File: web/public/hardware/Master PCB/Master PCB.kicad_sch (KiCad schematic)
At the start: 42 parts, among them J1 SWD Conn, SW1 nRST, U1 STM32U585VITx

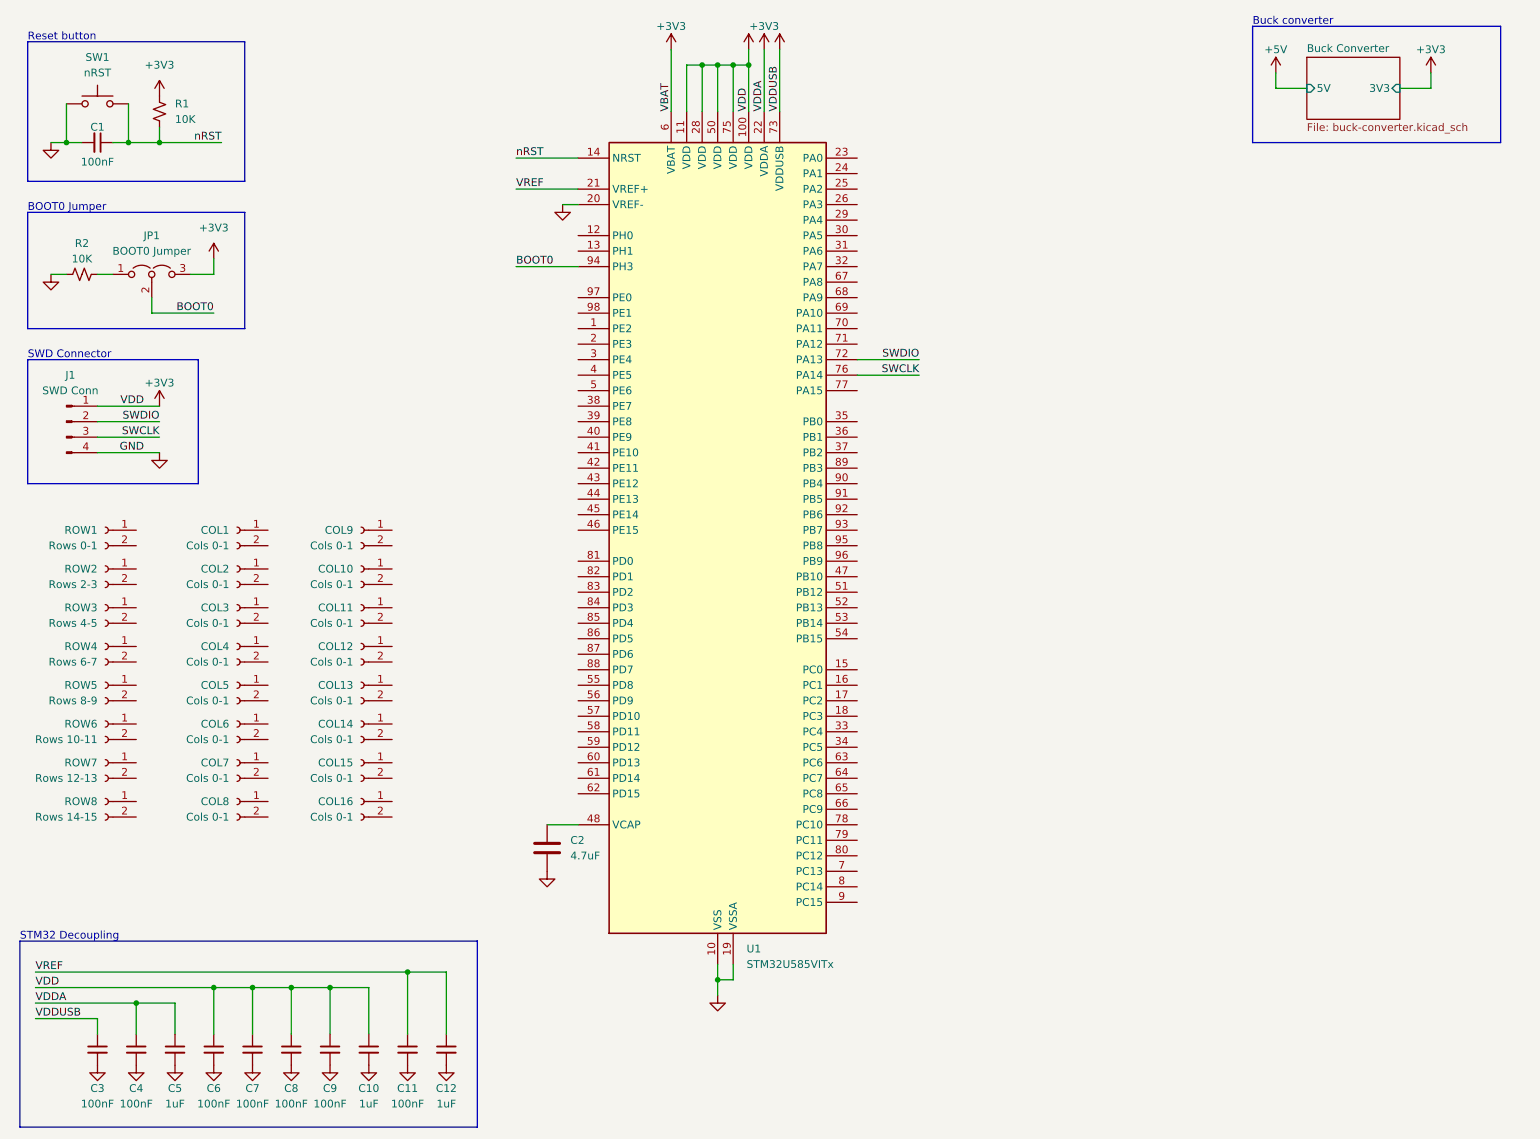
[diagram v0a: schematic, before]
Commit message: Add row/column headers, some hierarchical sheets
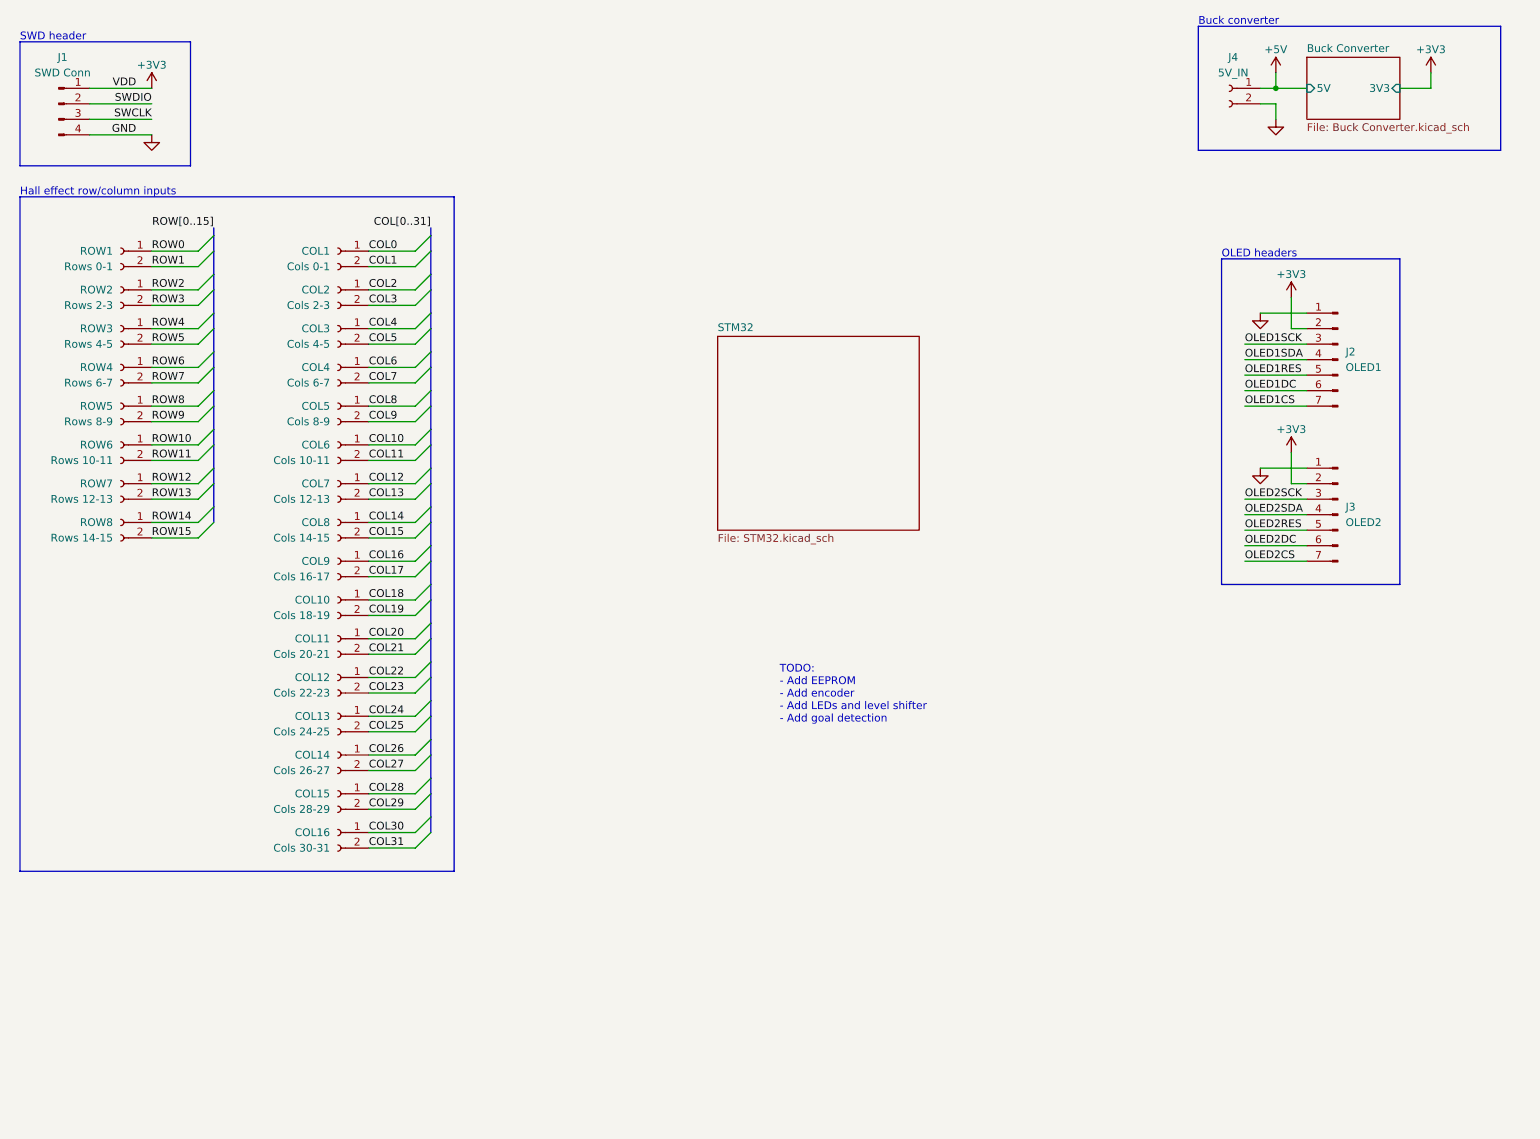
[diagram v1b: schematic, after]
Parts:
- removed C1, C11, C3, C4, C6, C7, C8, C9: 100nF, symbol Device:C_Small
- removed C10, C12, C5: 1uF, symbol Device:C_Small
- removed C2: 4.7uF, symbol Device:C
- removed JP1: BOOT0 Jumper, symbol Jumper:Jumper_3_Open
- removed R1, R2: 10K, symbol Device:R_Small_US
- removed SW1: nRST, symbol Switch:SW_Push
- removed U1: STM32U585VITx, Package_QFP:LQFP-100_14x14mm_P0.5mm, symbol MCU_ST_STM32U5:STM32U585VITx
- added J2: OLED1, symbol Connector:Conn_01x07_Pin
- added J3: OLED2, symbol Connector:Conn_01x07_Pin
- added J4: 5V_IN, symbol Connector:Conn_01x02_Socket
- COL10: value Cols 0-1 -> Cols 18-19
- COL11: value Cols 0-1 -> Cols 20-21
- COL12: value Cols 0-1 -> Cols 22-23
- COL13: value Cols 0-1 -> Cols 24-25
- COL14: value Cols 0-1 -> Cols 26-27
- COL15: value Cols 0-1 -> Cols 28-29
- COL16: value Cols 0-1 -> Cols 30-31
- COL2: value Cols 0-1 -> Cols 2-3
- COL3: value Cols 0-1 -> Cols 4-5
- COL4: value Cols 0-1 -> Cols 6-7
- COL5: value Cols 0-1 -> Cols 8-9
- COL6: value Cols 0-1 -> Cols 10-11
- COL7: value Cols 0-1 -> Cols 12-13
- COL8: value Cols 0-1 -> Cols 14-15
- COL9: value Cols 0-1 -> Cols 16-17
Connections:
- net +3V3: now also J2.2 (Pin_2), J3.2 (Pin_2)
- net +5V: now also J4.1 (Pin_1)
- net GND: now also J2.1 (Pin_1), J3.1 (Pin_1), J4.2 (Pin_2)
- net ROW6: now reaches ROW4.1 (Pin_1)
- net ROW7: now reaches ROW4.2 (Pin_2)
- net ROW2: now reaches ROW2.1 (Pin_1)
- net ROW3: now reaches ROW2.2 (Pin_2)
- net ROW10: now reaches ROW6.1 (Pin_1)
- net ROW11: now reaches ROW6.2 (Pin_2)
- net COL0: now reaches COL1.1 (Pin_1)
- net COL1: now reaches COL1.2 (Pin_2)
- net COL2: now reaches COL2.1 (Pin_1)
- net COL3: now reaches COL2.2 (Pin_2)
- net COL12: now reaches COL7.1 (Pin_1)
- net COL13: now reaches COL7.2 (Pin_2)
- net COL24: now reaches COL13.1 (Pin_1)
- net COL25: now reaches COL13.2 (Pin_2)
- net ROW0: now reaches ROW1.1 (Pin_1)
- net ROW1: now reaches ROW1.2 (Pin_2)
- net COL10: now reaches COL6.1 (Pin_1)
- net COL11: now reaches COL6.2 (Pin_2)
- net COL22: now reaches COL12.1 (Pin_1)
- net COL23: now reaches COL12.2 (Pin_2)
- net COL26: now reaches COL14.1 (Pin_1)
- net COL27: now reaches COL14.2 (Pin_2)
- net COL8: now reaches COL5.1 (Pin_1)
- net COL9: now reaches COL5.2 (Pin_2)
- net COL28: now reaches COL15.1 (Pin_1)
- net COL29: now reaches COL15.2 (Pin_2)
- net ROW12: now reaches ROW7.1 (Pin_1)
- net ROW13: now reaches ROW7.2 (Pin_2)
- net COL18: now reaches COL10.1 (Pin_1)
- net COL19: now reaches COL10.2 (Pin_2)
- net COL4: now reaches COL3.1 (Pin_1)
- net COL5: now reaches COL3.2 (Pin_2)
- net ROW14: now reaches ROW8.1 (Pin_1)
- net ROW15: now reaches ROW8.2 (Pin_2)
- net ROW4: now reaches ROW3.1 (Pin_1)
- net ROW5: now reaches ROW3.2 (Pin_2)
- net COL20: now reaches COL11.1 (Pin_1)
- net COL21: now reaches COL11.2 (Pin_2)
- net COL6: now reaches COL4.1 (Pin_1)
- net COL7: now reaches COL4.2 (Pin_2)
- net COL16: now reaches COL9.1 (Pin_1)
- net COL17: now reaches COL9.2 (Pin_2)
- net ROW8: now reaches ROW5.1 (Pin_1)
- net ROW9: now reaches ROW5.2 (Pin_2)
- net COL14: now reaches COL8.1 (Pin_1)
- net COL15: now reaches COL8.2 (Pin_2)
- net COL30: now reaches COL16.1 (Pin_1)
- net COL31: now reaches COL16.2 (Pin_2)
- new net OLED1CS: J2.7 (Pin_7)
- new net OLED1DC: J2.6 (Pin_6)
- new net OLED1RES: J2.5 (Pin_5)
- new net OLED1SCK: J2.3 (Pin_3)
- new net OLED1SDA: J2.4 (Pin_4)
- new net OLED2CS: J3.7 (Pin_7)
- new net OLED2DC: J3.6 (Pin_6)
- new net OLED2RES: J3.5 (Pin_5)
- new net OLED2SCK: J3.3 (Pin_3)
- new net OLED2SDA: J3.4 (Pin_4)
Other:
- added sheet STM32 (STM32.kicad_sch)
- sheet Buck Converter: file buck-converter.kicad_sch -> Buck Converter.kicad_sch
- note added: "Hall effect row/column inputs"
- note added: "OLED headers"
- note added: "SWD header"
- note added: "TODO: - Add EEPROM - Add encoder - Add LEDs and level shifter - Add goal detection"
- note removed: "BOOT0 Jumper"
- note removed: "Reset button"
- note removed: "STM32 Decoupling"
- note removed: "SWD Connector"
- moved on the sheet: COL1, COL10, COL11, COL12, COL13, COL14, COL15, COL16, COL2, COL3, COL4, COL5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

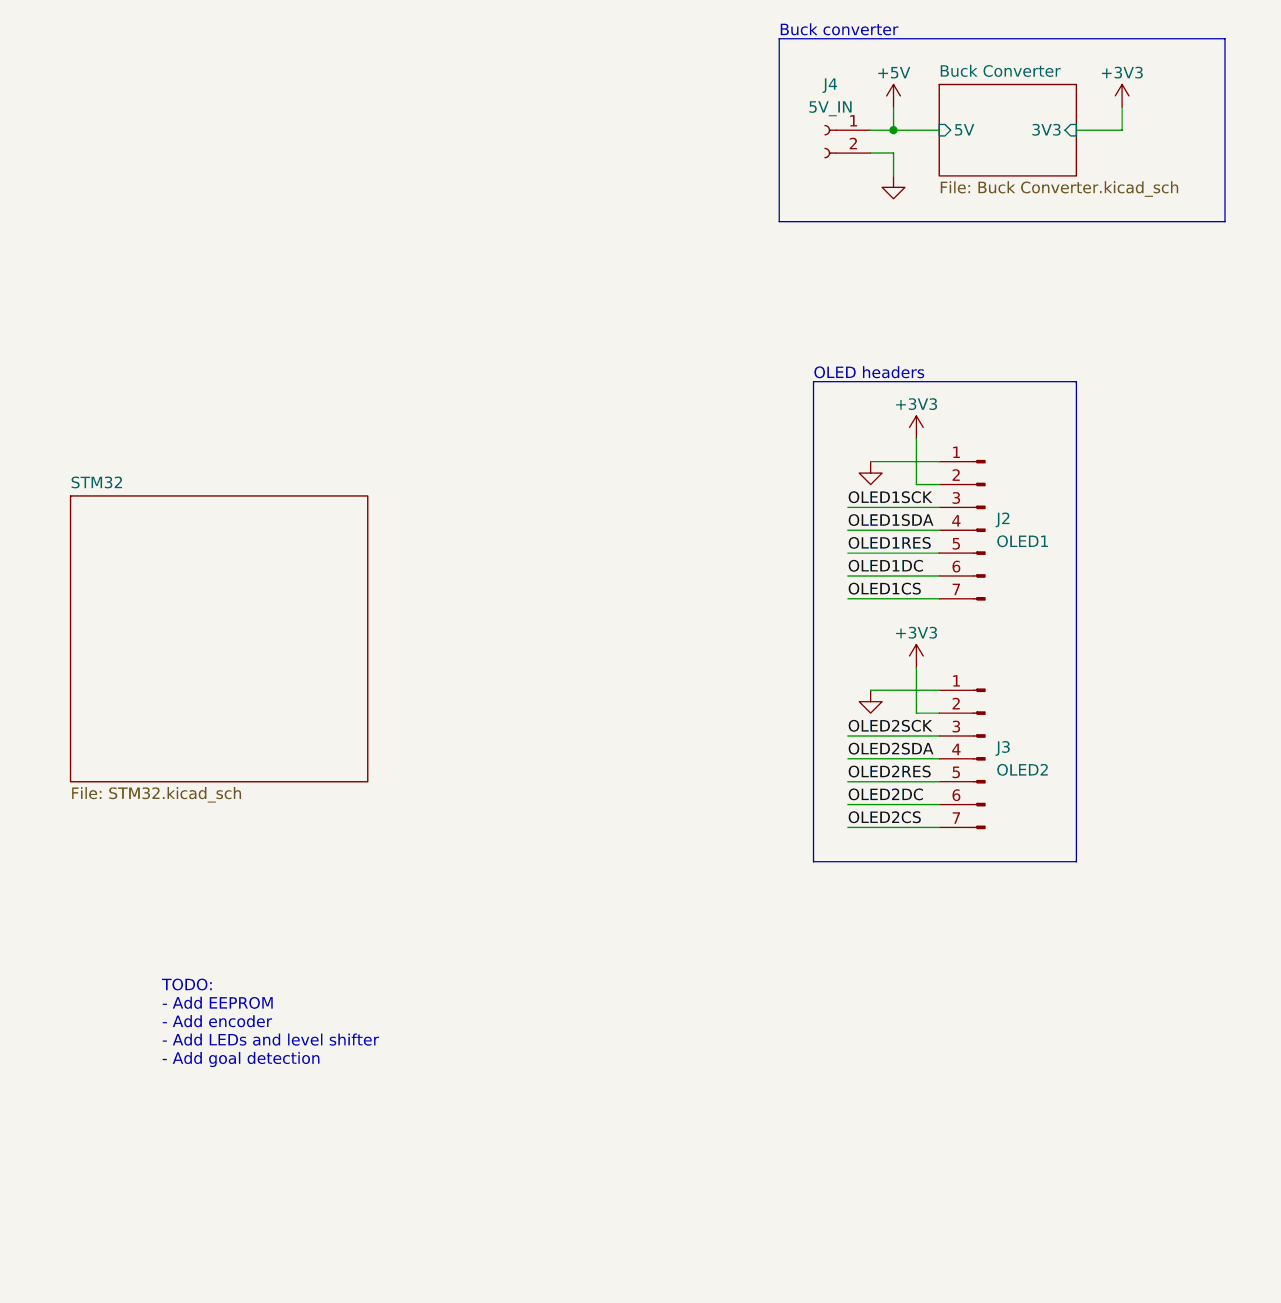
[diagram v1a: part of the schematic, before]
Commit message: Add EEPROM
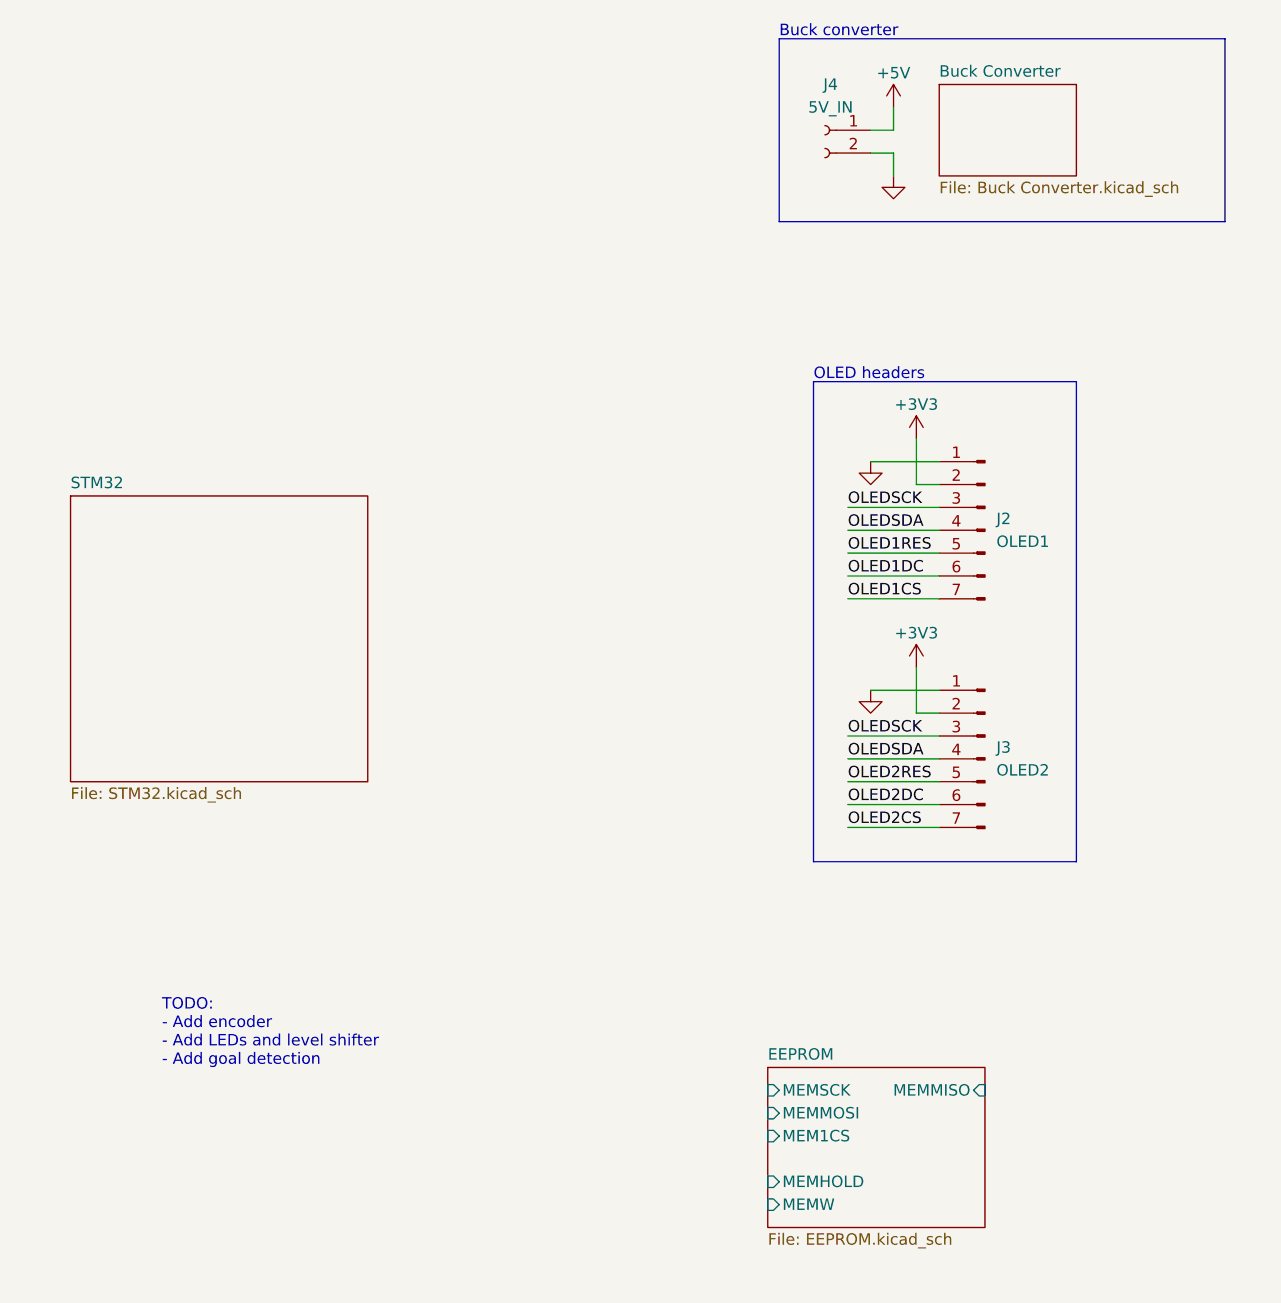
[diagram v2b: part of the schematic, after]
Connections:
- net OLED2SCK is gone; now on net OLEDSCK: J3.3 (Pin_3)
- net OLED2SDA is gone; now on net OLEDSDA: J3.4 (Pin_4)
- net OLED1SCK renamed OLEDSCK
- net OLED1SDA renamed OLEDSDA
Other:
- added sheet EEPROM (EEPROM.kicad_sch)
- sheet Buck Converter ports: added none; removed 3V3, 5V
- note added: "TODO: - Add encoder - Add LEDs and level shifter - Add goal detection"
- note removed: "TODO: - Add EEPROM - Add encoder - Add LEDs and level shifter - Add goal detection"

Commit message: Add encoder
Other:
- added sheet Menu Encoder (Menu Encoder.kicad_sch)
- note added: "TODO: - Add LEDs and level shifter - Add goal detection"
- note removed: "TODO: - Add encoder - Add LEDs and level shifter - Add goal detection"
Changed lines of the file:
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@@
     (effects (font (size 1.27 1.27)) (justify left bottom))
   )
-  (text "TODO:\n- Add encoder\n- Add LEDs and level shifter\n- Add goal detection"
+  (text "TODO:\n- Add LEDs and level shifter\n- Add goal detection"
     (at 143.51 132.08 0)
     (effects (font (size 1.27 1.27)) (justify left bottom))
@@
       )
     )
+  )
+  (sheet (at 157.48 149.86) (size 12.7 10.16) (fields_autoplaced)
+    (stroke (width 0.1524) (type solid))
+    (fill (color 0 0 0 0.0000))
+    (property "Sheetname" "Menu Encoder" (at 157.48 149.1484 0)
+      (effects (font (size 1.27 1.27)) (justify left bottom))
+    )
+    (property "Sheetfile" "Menu Encoder.kicad_sch" (at 157.48 160.6046 0)
+      (effects (font (size 1.27 1.27)) (justify left top))
+    )
+    (pin "A" input (at 157.48 152.4 180)
+      (effects (font (size 1.27 1.27)) (justify left))
+    )
+    (pin "B" input (at 157.48 154.94 180)
+      (effects (font (size 1.27 1.27)) (justify left))
+    )
+    (pin "SW" input (at 157.48 157.48 180)
+      (effects (font (size 1.27 1.27)) (justify left))
+    )
+    (instances
+      (project "Master PCB"
+        (path "/61606422-4f73-4717-9ce6-6ac5e634e7ae" (page "5"))
+      )
+    )

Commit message: Add LED level shifters
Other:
- added sheet LED (LED.kicad_sch)
- note added: "TODO: - Add goal detection"
- note removed: "TODO: - Add LEDs and level shifter - Add goal detection"
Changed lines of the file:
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@@
     (effects (font (size 1.27 1.27)) (justify left bottom))
   )
-  (text "TODO:\n- Add LEDs and level shifter\n- Add goal detection"
-    (at 143.51 132.08 0)
+  (text "TODO:\n- Add goal detection" (at 143.51 132.08 0)
     (effects (font (size 1.27 1.27)) (justify left bottom))
   )
@@
       )
     )
+  )
+  (sheet (at 179.07 102.87) (size 21.59 12.7) (fields_autoplaced)
+    (stroke (width 0.1524) (type solid))
+    (fill (color 0 0 0 0.0000))
+    (property "Sheetname" "LED" (at 179.07 102.1584 0)
+      (effects (font (size 1.27 1.27)) (justify left bottom))
+    )
+    (property "Sheetfile" "LED.kicad_sch" (at 179.07 116.1546 0)
+      (effects (font (size 1.27 1.27)) (justify left top))
+    )
+    (pin "LED1IN" input (at 179.07 105.41 180)
+      (effects (font (size 1.27 1.27)) (justify left))
+    )
+    (pin "LED2IN" input (at 179.07 107.95 180)
+      (effects (font (size 1.27 1.27)) (justify left))
+    )
+    (pin "LED2OUT" input (at 200.66 107.95 0)
+      (effects (font (size 1.27 1.27)) (justify right))
+    )
+    (pin "LED1OUT" input (at 200.66 105.41 0)
+      (effects (font (size 1.27 1.27)) (justify right))
+    )
+    (pin "LED3OUT" input (at 200.66 110.49 0)
+      (effects (font (size 1.27 1.27)) (justify right))
+    )
+    (pin "LED3IN" input (at 179.07 110.49 180)
+      (effects (font (size 1.27 1.27)) (justify left))
+    )
+    (pin "LED4IN" input (at 179.07 113.03 180)
+      (effects (font (size 1.27 1.27)) (justify left))
+    )
+    (pin "LED4OUT" input (at 200.66 113.03 0)
+      (effects (font (size 1.27 1.27)) (justify right))
+    )
+    (instances
+      (project "Master PCB"
+        (path "/61606422-4f73-4717-9ce6-6ac5e634e7ae" (page "6"))
+      )
+    )
